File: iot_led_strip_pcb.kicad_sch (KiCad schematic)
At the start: 35 parts, among them J1 I2C Expansion, J2 Conn_01x03_Socket, J3 GT-USB-7010ASV, J4 Barrel_Jack_Switch_Pin3Ring, J5 TC2050-IDC_Cortex-M, J6 Conn_01x03_Socket_Solderwire, J8 UART, Q1 BSS138, SW1 RESET, SW2 FLASH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

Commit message: lots of small changes. Schematic updated with mic, layout not yet
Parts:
- removed C8, C9: 47pF, Capacitor_SMD:C_0805_2012Metric_Pad1.18x1.45mm_HandSolder, symbol Device:C
- added C7: 100nF, Capacitor_SMD:C_0805_2012Metric_Pad1.18x1.45mm_HandSolder, symbol Device:C
- added JP1: MIC_CLK_SEL, symbol Jumper:SolderJumper_3_Bridged12
- added MK1: SPH0641LU4H-1, Sensor_Audio:Knowles_LGA-5_3.5x2.65mm, symbol Sensor_Audio:SPH0641LU4H-1
- added R6: 100, Resistor_SMD:R_0805_2012Metric_Pad1.20x1.40mm_HandSolder, symbol Device:R_US
- R10: LCSC (none) -> C17594; Vendor FILLME -> https://www.lcsc.com/product-detail/Chip-Resistor-Surface-M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
- R3: LCSC (none) -> C17594; Vendor (none) -> https://www.lcsc.com/product-detail/Chip-Resistor-Surface-M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
- SW1, SW2: footprint Button_Switch_SMD:SW_SPST_CK_RS282G05A3 -> Button_Switch_SMD:SW_SPST_TL3342
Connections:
- net +3.3V: now also C7.1, MK1.5 (VDD)
- net Earth: now also C7.2, MK1.3 (GND)
- net SCL: now also J1.3 (Pin_3); no longer J1.4 (Pin_4)
- net SDA: now also J1.4 (Pin_4); no longer J1.3 (Pin_3)
- net XP: now also JP1.1 (A)
- net MIC_CLK: now reaches U3.5 (GPIO5/TOUCH5/ADC1_CH4)
- net MIC_CLK: now also JP1.3 (B)
- net MIC_DATA: now reaches U3.6 (GPIO6/TOUCH6/ADC1_CH5)
- net MIC_DATA: now also R6.1
- new net: JP1.2 (C), MK1.4 (CLOCK)
- new net: MK1.1 (DATA), R6.2
- no-connect marks 25 -> 24
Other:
- note added: "3 pin connector with strain relief"
- note added: "Normal 3 pin header 2.54mm spacing"
- note added: "Optional MEMS Microphone"
- note removed: "* re-do esp32 footprint so it's handsolderable * add usb-uart port * check and re-fill in values for passives"
- note removed: "TODO"

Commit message: microphone added to layout, DRC passes
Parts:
- JP1: footprint (none) -> Jumper:SolderJumper-3_P1.3mm_Bridged12_RoundedPad1.0x1.5mm
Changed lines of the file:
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@@
       (effects (font (size 1.27 1.27)) (justify left))
     )
-    (property "Footprint" "" (at 169.545 32.385 0)
+    (property "Footprint" "Jumper:SolderJumper-3_P1.3mm_Bridged12_RoundedPad1.0x1.5mm" (at 169.545 32.385 0)
       (effects (font (size 1.27 1.27)) hide)
     )

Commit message: v2.1 export, renders
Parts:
- JP1: now left out of the parts list
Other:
- note added: "Logic Level Shifter"
- note removed: "NeoPixel LED Driver"
- moved on the sheet: C10, C11, C14, D5, J1, J8, R12, R4, R5, SW1, SW2, Y1

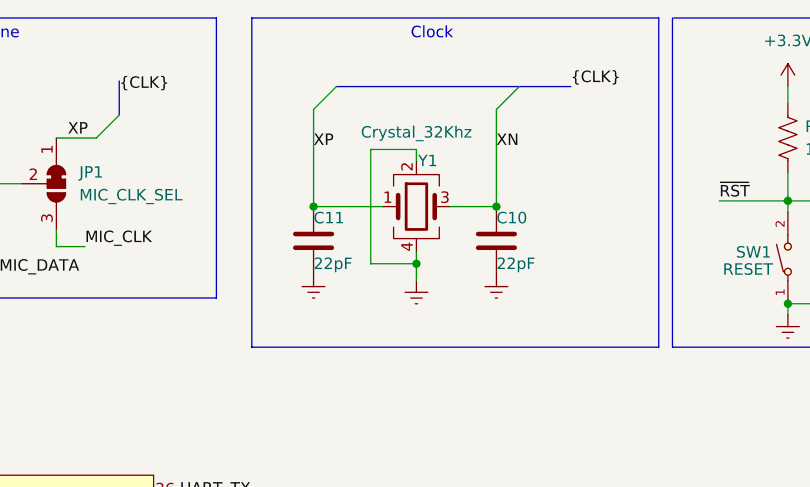
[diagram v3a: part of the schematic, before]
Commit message: replaced crystal. re-updated all renders and images
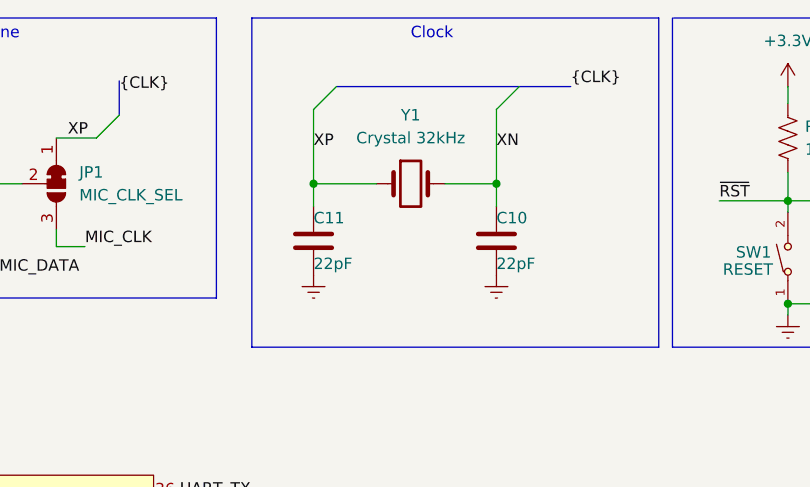
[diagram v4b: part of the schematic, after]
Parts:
- removed Y1: Crystal_32Khz, Crystal:Crystal_SMD_3225-4Pin_3.2x2.5mm_HandSoldering, symbol Device:Crystal_GND24
- added Y1: Crystal 32kHz, Crystal:Crystal_SMD_3215-2Pin_3.2x1.5mm, symbol Device:Crystal
- MK1: LCSC (none) -> C5454543; Vendor (none) -> https://www.lcsc.com/product-detail/MEMS-Microphones_Knowle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
- U3: LCSC (none) -> C3040594
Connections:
- net XN: now also Y1.2
- net XP: now also Y1.1
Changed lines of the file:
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@@
   (junction (at 41.275 30.48) (diameter 0) (color 0 0 0 0)
   )
-  (junction (at 198.12 34.925) (diameter 0) (color 0 0 0 0)
+  (junction (at 198.12 32.385) (diameter 0) (color 0 0 0 0)
   )
   (junction (at 200.66 125.73) (diameter 0) (color 0 0 0 0)
@@
   (junction (at 137.16 53.34) (diameter 0) (color 0 0 0 0)
   )
-  (junction (at 209.55 41.275) (diameter 0) (color 0 0 0 0)
+  (junction (at 218.44 32.385) (diameter 0) (color 0 0 0 0)
   )
   (junction (at 144.145 20.955) (diameter 0) (color 0 0 0 0)
@@
   )
   (junction (at 19.05 147.32) (diameter 0) (color 0 0 0 0)
-  )
-  (junction (at 218.44 34.925) (diameter 0) (color 0 0 0 0)
   )
   (junction (at 45.72 137.16) (diameter 0) (color 0 0 0 0)
@@
     (stroke (width 0) (type default))
   )
-  (wire (pts (xy 209.55 41.275) (xy 209.55 43.18))
-    (stroke (width 0) (type default))
-  )
   (wire (pts (xy 86.995 23.495) (xy 86.995 30.48))
     (stroke (width 0) (type default))
@@
     (stroke (width 0) (type default))
   )
-  (wire (pts (xy 198.12 34.925) (xy 205.74 34.925))
-    (stroke (width 0) (type default))
-  )
   (wire (pts (xy 41.91 132.08) (xy 45.72 132.08))
     (stroke (width 0) (type default))
@@
     (stroke (width 0) (type default))
   )
-  (wire (pts (xy 204.47 41.275) (xy 209.55 41.275))
-    (stroke (width 0) (type default))
-  )
   (wire (pts (xy 182.88 87.63) (xy 185.42 87.63))
     (stroke (width 0) (type default))
@@
     (stroke (width 0) (type default))
   )
+  (wire (pts (xy 218.44 32.385) (xy 218.44 34.925))
+    (stroke (width 0) (type default))
+  )
   (wire (pts (xy 34.925 188.595) (xy 34.925 184.15))
     (stroke (width 0) (type default))
@@
     (stroke (width 0) (type default))
   )
-  (wire (pts (xy 209.55 29.845) (xy 209.55 28.575))
-    (stroke (width 0) (type default))
-  )
   (wire (pts (xy 250.825 34.29) (xy 250.825 35.56))
     (stroke (width 0) (type default))
@@
     (stroke (width 0) (type default))
   )
-  (wire (pts (xy 218.44 24.13) (xy 218.44 34.925))
+  (wire (pts (xy 218.44 24.13) (xy 218.44 32.385))
     (stroke (width 0) (type default))
   )
@@
     (stroke (width 0) (type default))
   )
+  (wire (pts (xy 198.12 32.385) (xy 198.12 34.925))
+    (stroke (width 0) (type default))
+  )
   (wire (pts (xy 73.66 134.62) (xy 80.645 134.62))
     (stroke (width 0) (type default))
@@
     (stroke (width 0) (type default))
   )
-  (wire (pts (xy 198.12 24.13) (xy 198.12 34.925))
+  (wire (pts (xy 198.12 24.13) (xy 198.12 32.385))
     (stroke (width 0) (type default))
   )
@@
     (stroke (width 0) (type default))
   )
-  (wire (pts (xy 209.55 28.575) (xy 204.47 28.575))
-    (stroke (width 0) (type default))
-  )
   (wire (pts (xy 86.995 77.47) (xy 91.44 77.47))
     (stroke (width 0) (type default))
   )
-  (wire (pts (xy 204.47 28.575) (xy 204.47 41.275))
-    (stroke (width 0) (type default))
-  )
   (wire (pts (xy 218.44 125.73) (xy 218.44 125.095))
     (stroke (width 0) (type default))
@@
     (stroke (width 0) (type default))
   )
+  (wire (pts (xy 198.12 32.385) (xy 205.105 32.385))
+    (stroke (width 0) (type default))
+  )
   (wire (pts (xy 182.88 125.73) (xy 200.66 125.73))
     (stroke (width 0) (type default))
@@
     (stroke (width 0) (type default))
   )
-  (wire (pts (xy 213.36 34.925) (xy 218.44 34.925))
+  (wire (pts (xy 212.725 32.385) (xy 218.44 32.385))
     (stroke (width 0) (type default))
   )
@@
   )
   (wire (pts (xy 41.91 124.46) (xy 43.18 124.46))
-    (stroke (width 0) (type default))
-  )
-  (wire (pts (xy 209.55 40.005) (xy 209.55 41.275))
     (stroke (width 0) (type default))
   )
@@
     )
   )
+  (symbol (lib_id "Device:Crystal") (at 208.915 32.385 0) (unit 1)
+    (in_bom yes) (on_board yes) (dnp no) (fields_autoplaced)
+    (property "Reference" "Y1" (at 208.915 24.765 0)
+      (effects (font (size 1.27 1.27)))
+    )
+    (property "Value" "Crystal 32kHz" (at 208.915 27.305 0)
+      (effects (font (size 1.27 1.27)))
+    )
+    (property "Footprint" "Crystal:Crystal_SMD_3215-2Pin_3.2x1.5mm" (at 208.915 32.385 0)
+      (effects (font (size 1.27 1.27)) hide)
+    )
+    (property "Datasheet" "~" (at 208.915 32.385 0)
+      (effects (font (size 1.27 1.27)) hide)
+    )
+    (property "LCSC" "C97606" (at 208.915 32.385 0)
+      (effects (font (size 1.27 1.27)) hide)
+    )
+    (pin "1")
+    (pin "2")
+    (instances
+      (project "iot_led_strip_pcb"
+        (path "/745f5767-ebad-4719-b66e-073bc90db4bc"
+          (reference "Y1") (unit 1)
+        )
+      )
+    )
+  )
   (symbol (lib_id "power:Earth") (at 52.705 139.7 0) (mirror y) (unit 1)
     (in_bom yes) (on_board yes) (dnp no) (fields_autoplaced)
@@
         (path "/745f5767-ebad-4719-b66e-073bc90db4bc"
           (reference "#PWR033") (unit 1)
-        )
-      )
-    )
-  )
-  (symbol (lib_id "Device:Crystal_GND24") (at 209.55 34.925 0) (unit 1)
-    (in_bom yes) (on_board yes) (dnp no)
-    (property "Reference" "Y1" (at 210.82 29.845 0)
-      (effects (font (size 1.27 1.27)))
-    )
-    (property "Value" "Crystal_32Khz" (at 209.55 26.67 0)
-      (effects (font (size 1.27 1.27)))
-    )
-    (property "Footprint" "Crystal:Crystal_SMD_3225-4Pin_3.2x2.5mm_HandSoldering" (at 209.55 34.925 0)
-      (effects (font (size 1.27 1.27)) hide)
-    )
-    (property "Datasheet" "~" (at 209.55 34.925 0)
-      (effects (font (size 1.27 1.27)) hide)
-    )
-    (property "Vendor" "FILLME" (at 209.55 34.925 0)
-      (effects (font (size 1.27 1.27)) hide)
-    )
-    (property "LCSC" "" (at 209.55 34.925 0)
-      (effects (font (size 1.27 1.27)) hide)
-    )
-    (pin "1")
-    (pin "2")
-    (pin "3")
-    (pin "4")
-    (instances
-      (project "iot_led_strip_pcb"
-        (path "/745f5767-ebad-4719-b66e-073bc90db4bc"
-          (reference "Y1") (unit 1)
         )
       )
@@
       (effects (font (size 1.27 1.27)) hide)
     )
+    (property "LCSC" "C5454543" (at 144.145 32.385 0)
+      (effects (font (size 1.27 1.27)) hide)
+    )
+    (property "Vendor" "https://www.lcsc.com/product-detail/MEMS-Microphones_Knowles-SPH0641LM4H-1-8_C5454543.html" (at 144.145 32.385 0)
+      (effects (font (size 1.27 1.27)) hide)
+    )
     (pin "1")
     (pin "2")
@@
     )
     (property "Datasheet" "https://www.espressif.com/sites/default/files/documentation/esp32-s2-solo_esp32-s2-solo-u_datasheet_en.pdf" (at 137.16 161.29 0)
+      (effects (font (size 1.27 1.27)) hide)
+    )
+    (property "LCSC" "C3040594" (at 137.16 105.41 0)
       (effects (font (size 1.27 1.27)) hide)
     )
@@
         )
       )
-    )
-  )
-  (symbol (lib_id "power:Earth") (at 209.55 43.18 0) (mirror y) (unit 1)
-    (in_bom yes) (on_board yes) (dnp no) (fields_autoplaced)
-    (property "Reference" "#PWR04" (at 209.55 49.53 0)
-      (effects (font (size 1.27 1.27)) hide)
-    )
-    (property "Value" "Earth" (at 209.55 46.99 0)
-      (effects (font (size 1.27 1.27)) hide)
-    )
-    (property "Footprint" "" (at 209.55 43.18 0)
-      (effects (font (size 1.27 1.27)) hide)
-    )
-    (property "Datasheet" "~" (at 209.55 43.18 0)
-      (effects (font (size 1.27 1.27)) hide)
-    )
-    (pin "1")
-    (instances
-      (project "iot_led_strip_pcb"
-        (path "/745f5767-ebad-4719-b66e-073bc90db4bc"
-          (reference "#PWR04") (unit 1)
-        )
-      )

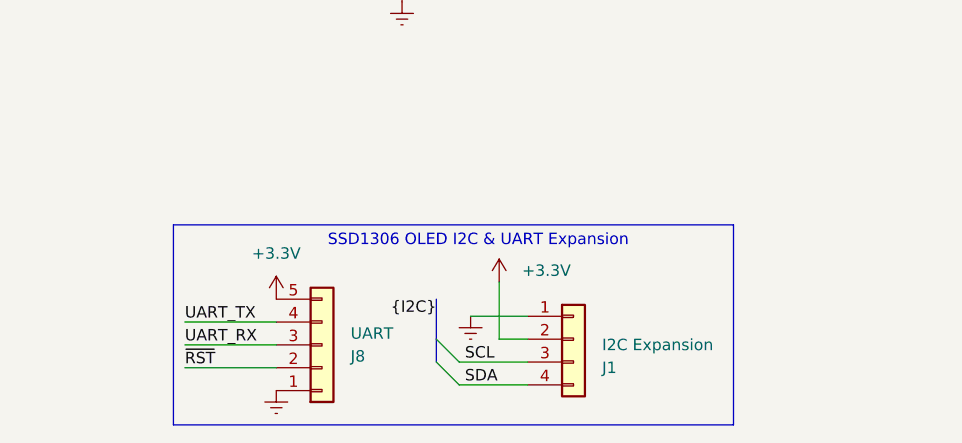
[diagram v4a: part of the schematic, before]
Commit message: some minor changes from during assembly and gif of assembled board added
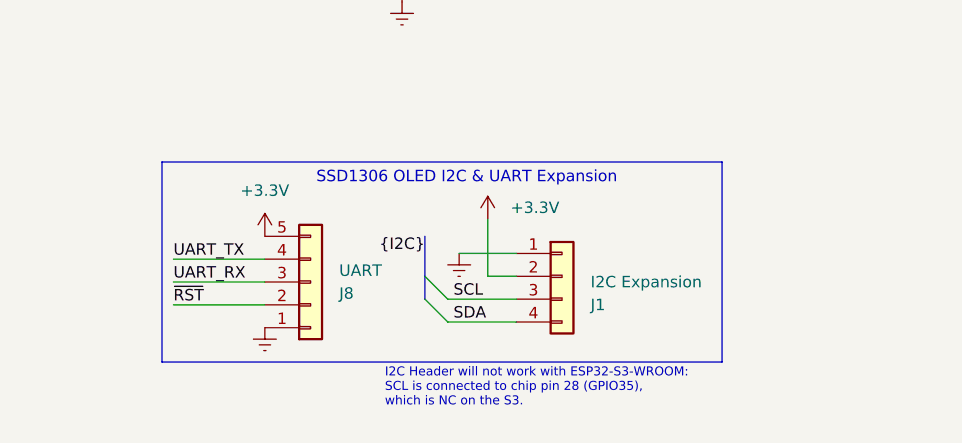
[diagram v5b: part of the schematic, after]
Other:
- note added: "I2C Header will not work with ESP32-S3-WROOM: SCL is connected to chip pin 28 (GPIO35), which is NC on the S3."
- moved on the sheet: J1, J8

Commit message: added power led disconnect and cleaned up some traces
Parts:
- added JP2: PWR_LED_BRIDGE, Jumper:SolderJumper-2_P1.3mm_Bridged_RoundedPad1.0x1.5mm, symbol Jumper:SolderJumper_2_Bridged
- D4: LCSC C84256 -> C2297; Vendor https://www.lcsc.com/product-detail/Light-Emitting-Diodes-L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 -> https://jlcpcb.com/partdetail/Hubei_KentoElec-KT0805G/C2297
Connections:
- net VBUS is gone; now on net +5V: J3.A4B9 (VBUS), J3.B4A9 (VBUS), J5.5 ((GND)/(Vcc5V))
- net +3.3V: now also JP2.2 (B); no longer R12.2
- new net: JP2.1 (A), R12.2
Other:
- sheet Power_and_board ports: added none; removed VBUS
- note added: "Jumper allows disabling of Power LED"
- moved on the sheet: D5, R12

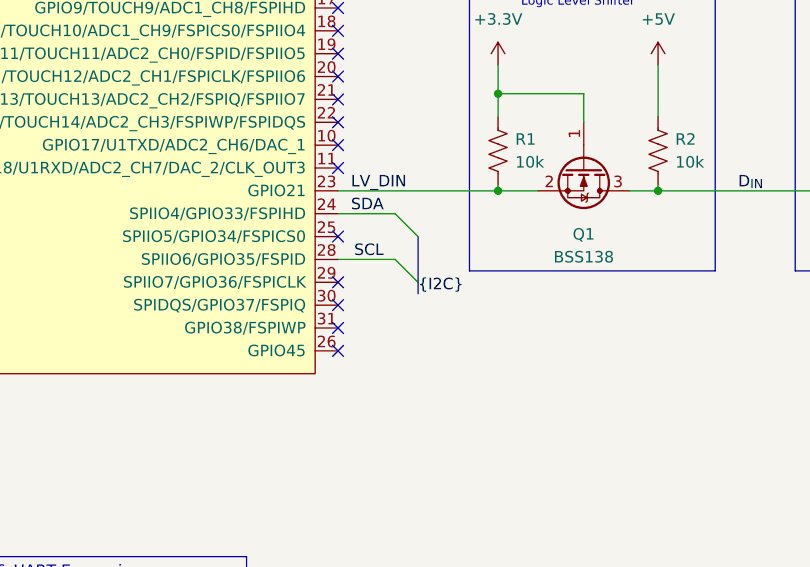
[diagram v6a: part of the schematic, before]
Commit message: moved i2c SCL to pin on both S2 and S3
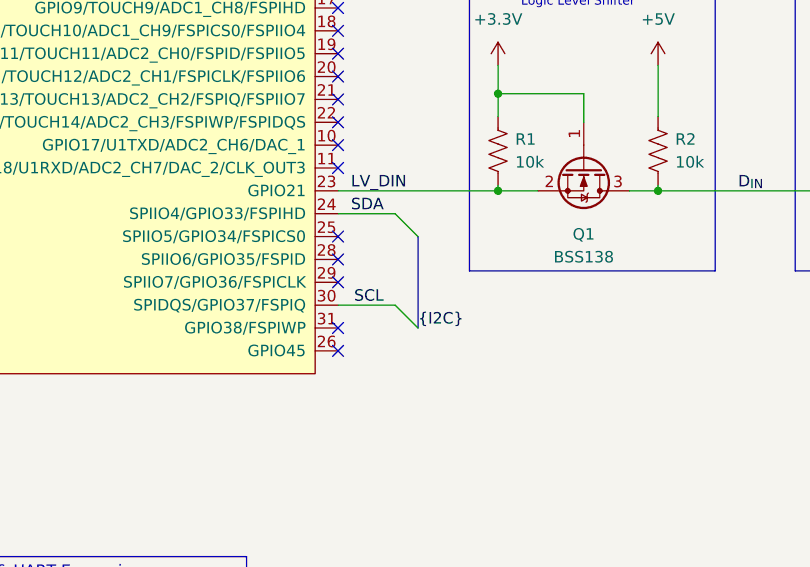
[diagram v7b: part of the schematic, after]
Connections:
- net SCL: now also U3.30 (SPIDQS/GPIO37/FSPIQ); no longer U3.28 (SPIIO6/GPIO35/FSPID)
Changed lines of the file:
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@@
   (no_connect (at 48.895 181.61))
   (no_connect (at 182.88 130.81))
+  (no_connect (at 182.88 133.35))
   (no_connect (at 182.88 110.49))
   (no_connect (at 48.895 176.53))
   (no_connect (at 182.88 143.51))
   (no_connect (at 182.88 135.89))
-  (no_connect (at 182.88 138.43))
   (no_connect (at 182.88 102.87))
   (no_connect (at 182.88 90.17))
@@
     (stroke (width 0) (type default))
   )
-  (bus_entry (at 189.23 133.35) (size 2.54 2.54)
+  (bus_entry (at 189.23 138.43) (size 2.54 2.54)
     (stroke (width 0) (type default))
   )
@@
     (stroke (width 0) (type default))
   )
-  (bus (pts (xy 191.77 130.81) (xy 191.77 135.89))
-    (stroke (width 0) (type default))
-  )
   (wire (pts (xy 41.91 121.92) (xy 45.72 121.92))
     (stroke (width 0) (type default))
@@
     (stroke (width 0) (type default))
   )
-  (wire (pts (xy 182.88 133.35) (xy 189.23 133.35))
+  (wire (pts (xy 182.88 138.43) (xy 189.23 138.43))
     (stroke (width 0) (type default))
   )
@@
     (stroke (width 0) (type default))
   )
-  (bus (pts (xy 191.77 135.89) (xy 191.77 137.16))
+  (bus (pts (xy 191.77 130.81) (xy 191.77 140.97))
     (stroke (width 0) (type default))
   )
@@
     (effects (font (size 1.27 1.27)) (justify left bottom))
   )
-  (label "{I2C}" (at 191.77 137.16 0) (fields_autoplaced)
+  (label "{I2C}" (at 191.77 140.97 0) (fields_autoplaced)
     (effects (font (size 1.27 1.27)) (justify left bottom))
   )
@@
     (effects (font (size 1.27 1.27)) (justify right bottom))
   )
-  (label "SCL" (at 187.96 133.35 180) (fields_autoplaced)
+  (label "SCL" (at 187.96 138.43 180) (fields_autoplaced)
     (effects (font (size 1.27 1.27)) (justify right bottom))
   )
@@
       (effects (font (size 1.27 1.27)) hide)
     )
-    (property "Description" "100Ω 0805 125mW Chip Resistor" (at 158.115 34.925 0)
+    (property "Description" "100Ω 0805 125mW Chip Resistor (R11,R12 1k recommended)" (at 158.115 34.925 0)
       (effects (font (size 1.27 1.27)) hide)
     )
@@
       (effects (font (size 1.27 1.27)) hide)
     )
-    (property "Description" "100Ω 0805 125mW Chip Resistor" (at 97.155 38.1 0)
+    (property "Description" "100Ω 0805 125mW Chip Resistor (R11,R12 1k recommended)" (at 97.155 38.1 0)
       (effects (font (size 1.27 1.27)) hide)
     )
@@
       (effects (font (size 1.27 1.27)) hide)
     )
-    (property "Description" "100Ω 0805 125mW Chip Resistor" (at 189.23 87.63 0)
-      (effects (font (size 1.27 1.27)) hide)
-    )
+    (property "Description" "100Ω 0805 125mW Chip Resistor (R11,R12 1k recommended)" (at 189.23 87.63 0)
+      (effects (font (size 1.27 1.27)) hide)
+    )
